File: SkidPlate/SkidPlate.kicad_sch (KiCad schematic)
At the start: 23 parts, among them J8 S4B-PH-SM4-TB, U1 AMS1117-3.3, U2 LSM6DSOX

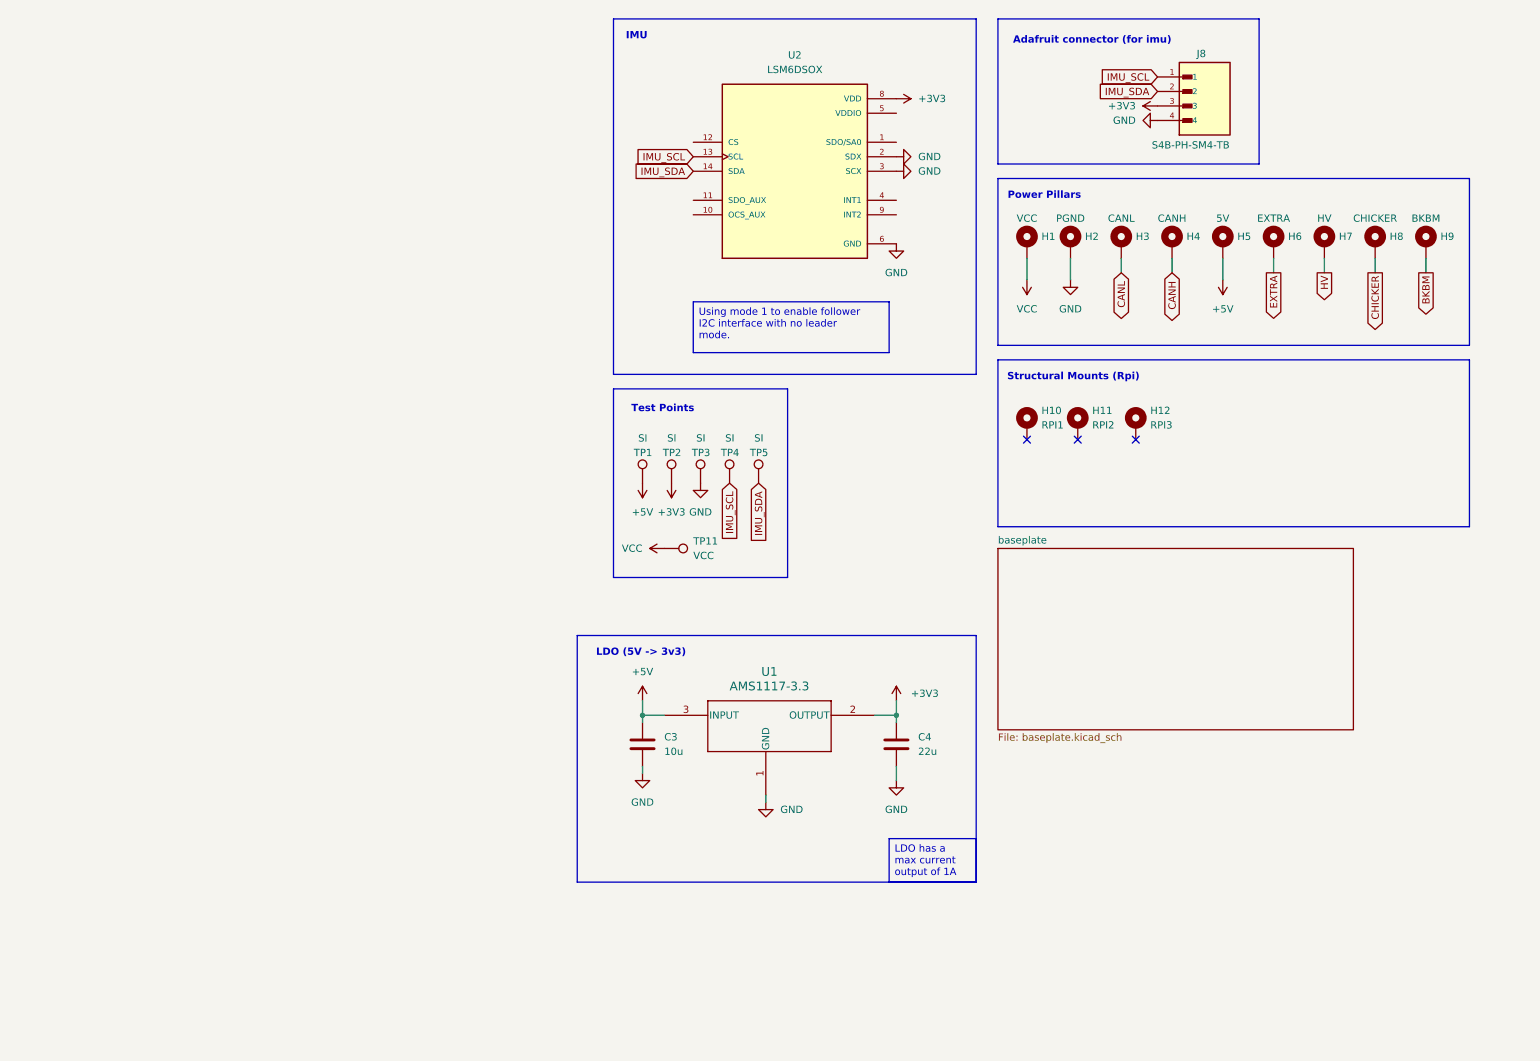
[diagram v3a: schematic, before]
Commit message: skidplate
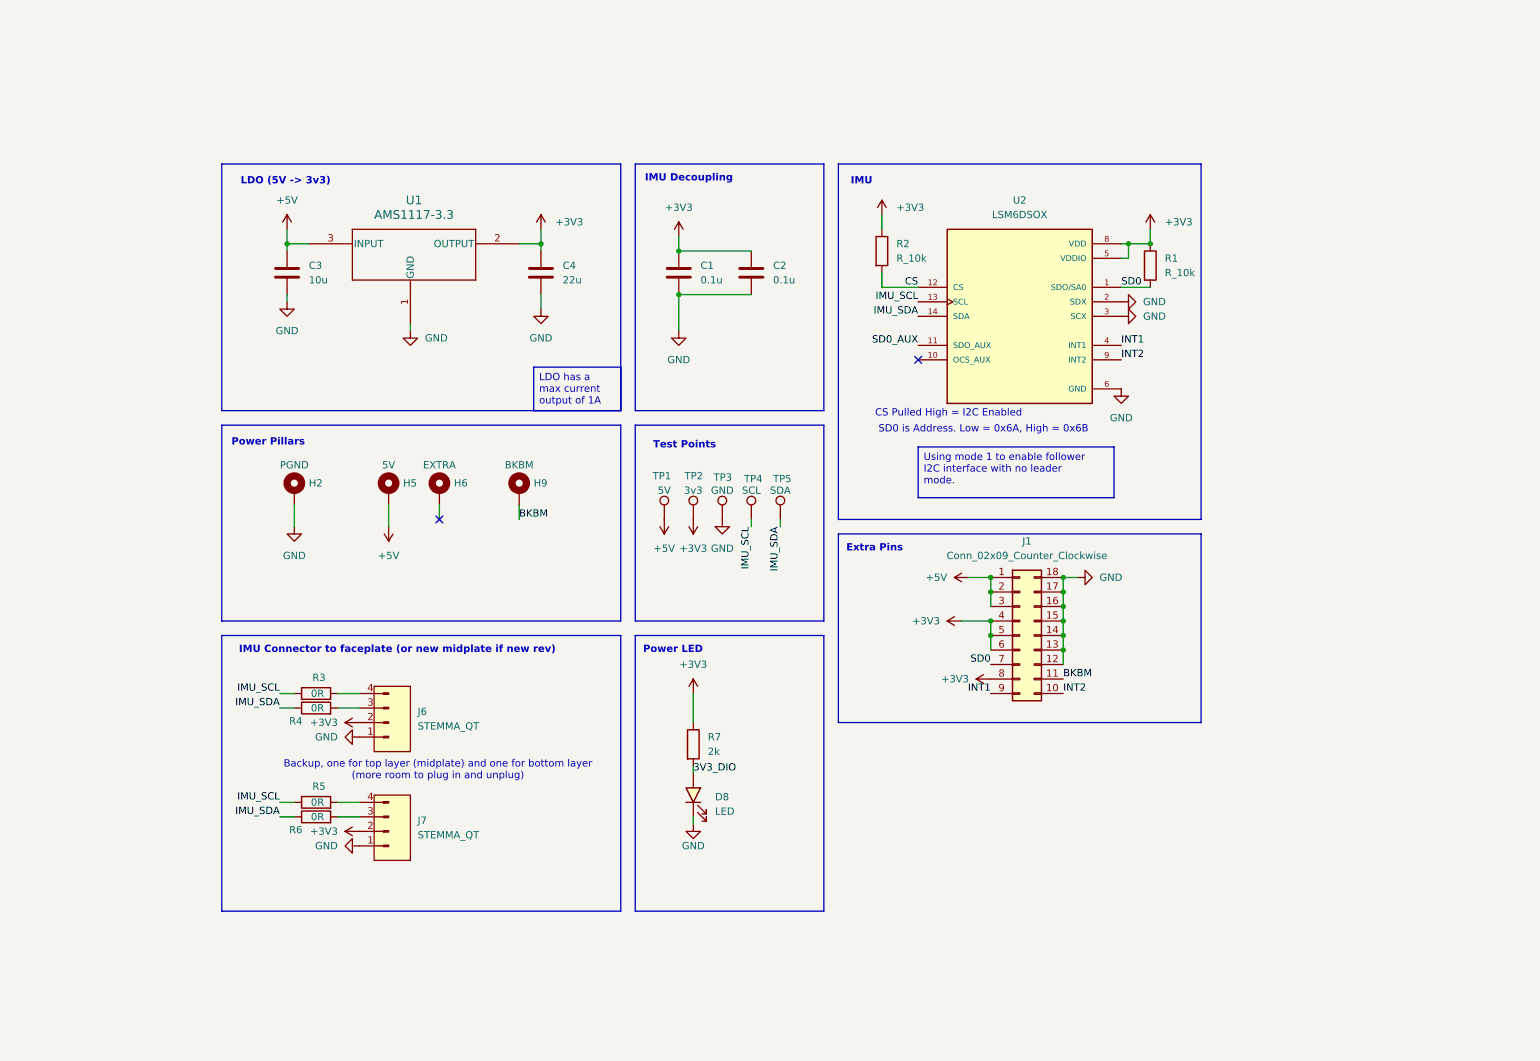
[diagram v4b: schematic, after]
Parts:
- removed H1: VCC, bots:MountingHole_2.7mm_M2.5_DIN965_Pad, symbol bots:MountingHoleM2.5NoThread_wConn
- removed H10: RPI1, bots:MountingHole_2.7mm_M2.5_DIN965_Pad, symbol bots:MountingHoleM2.5NoThread_wConn
- removed H11: RPI2, bots:MountingHole_2.7mm_M2.5_DIN965_Pad, symbol bots:MountingHoleM2.5NoThread_wConn
- removed H12: RPI3, bots:MountingHole_2.7mm_M2.5_DIN965_Pad, symbol bots:MountingHoleM2.5NoThread_wConn
- removed H3: CANL, bots:MountingHole_2.7mm_M2.5_DIN965_Pad, symbol bots:MountingHoleM2.5NoThread_wConn
- removed H4: CANH, bots:MountingHole_2.7mm_M2.5_DIN965_Pad, symbol bots:MountingHoleM2.5NoThread_wConn
- removed H7: HV, bots:MountingHole_2.7mm_M2.5_DIN965_Pad, symbol bots:MountingHoleM2.5NoThread_wConn
- removed H8: CHICKER, bots:MountingHole_2.7mm_M2.5_DIN965_Pad, symbol bots:MountingHoleM2.5NoThread_wConn
- removed J8: S4B-PH-SM4-TB, S4B-PH-SM4-TB:JST_S4B-PH-SM4-TB, symbol bots:S4B-PH-SM4-TB
- removed TP11: VCC, bots:TestPoint_Pad_2.0x2.0mm, symbol bots:TestPoint_2x2
- added C1, C2: 0.1u, bots:C_0603_1608Metric, symbol bots:C_0.1u
- added D8: LED, bots:LED_0805_2012Metric, symbol bots:LED_green
- added J1: Conn_02x09_Counter_Clockwise, bots:PinHeader_2x09_P2.54mm_Vertical, symbol bots:Conn_02x09_Counter_Clockwise
- added J6, J7: STEMMA_QT, bots:JST_SH_BM04B-SRSS-TB_1x04-1MP_P1.00mm_Vertical, symbol bots:STEMMA_QT
- added R1, R2: R_10k, bots:R_0603_1608Metric, symbol bots:R_10k
- added R3, R4, R5, R6: 0R, bots:R_0603_1608Metric, symbol bots:R_0R
- added R7: 2k, bots:R_0603_1608Metric, symbol bots:R_2k
- TP1: value SI -> 5V; footprint bots:pad_0603 -> bots:TestPoint_Pad_D1.0mm; symbol bots:TestPoint_1x1 -> bots:TestPoint1.0mm; now in the parts list
- TP2: value SI -> 3v3; footprint bots:pad_0603 -> bots:TestPoint_Pad_D1.0mm; symbol bots:TestPoint_1x1 -> bots:TestPoint1.0mm; now in the parts list
- TP3: value SI -> GND; footprint bots:pad_0603 -> bots:TestPoint_Pad_D1.0mm; symbol bots:TestPoint_1x1 -> bots:TestPoint1.0mm; now in the parts list
- TP4: value SI -> SCL; footprint bots:pad_0603 -> bots:TestPoint_Pad_D1.0mm; symbol bots:TestPoint_1x1 -> bots:TestPoint1.0mm; now in the parts list
- TP5: value SI -> SDA; footprint bots:pad_0603 -> bots:TestPoint_Pad_D1.0mm; symbol bots:TestPoint_1x1 -> bots:TestPoint1.0mm; now in the parts list
- U2: footprint bots:PQFN50P300X250X86-14N -> bots:PQFN50P250X300X86-14N; JLC (none) -> LGA-14(2.5x3); LCSC (none) -> C2655100
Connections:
- net +3V3: now also U2.5 (VDDIO), C1.1, C2.1, J1.4 (Pin_4), J1.5 (Pin_5), J1.6 (Pin_6), J1.8 (Pin_8), J6.2 (Pin_2), J7.2 (Pin_2), R1.1, R2.1, R7.1
- net +5V: now also J1.1 (Pin_1), J1.2 (Pin_2), J1.3 (Pin_3)
- net BKBM: now also J1.11 (Pin_11)
- net GND: now also C1.2, C2.2, D8.1 (K), J1.12 (Pin_12), J1.13 (Pin_13), J1.14 (Pin_14), J1.15 (Pin_15), J1.16 (Pin_16), J1.17 (Pin_17), J1.18 (Pin_18), J6.1 (Pin_1), J7.1 (Pin_1)
- net IMU_SCL: now also R3.1, R5.1
- net IMU_SDA: now also R4.1, R6.1
- net SD0: now reaches U2.1 (SDO/SA0)
- net SD0: now also J1.7 (Pin_7), R1.2
- net SD0_AUX: now reaches U2.11 (SDO_AUX)
- net CS: now reaches U2.12 (CS)
- net CS: now also R2.2
- net INT1: now reaches U2.4 (INT1)
- net INT1: now also J1.9 (Pin_9)
- net INT2: now reaches U2.9 (INT2)
- net INT2: now also J1.10 (Pin_10)
- net EXTRA: no longer names the net of H6.1
- new net: J6.3 (Pin_3), R4.2
- new net: J6.4 (Pin_4), R3.2
- new net: J7.3 (Pin_3), R6.2
- new net: J7.4 (Pin_4), R5.2
- new net 3V3_DIO: D8.2 (A), R7.2
- no-connect marks 3 -> 2
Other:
- removed sheet baseplate
- note added: "Backup, one for top layer (midplate) and one for bottom layer (more room to plug in and unplug)"
- note added: "CS Pulled High = I2C Enabled"
- note added: "Extra Pins"
- note added: "IMU Connector to faceplate (or new midplate if new rev)"
- note added: "IMU Decoupling"
- note added: "Power LED"
- note added: "SD0 is Address. Low = 0x6A, High = 0x6B"
- note removed: "Adafruit connector (for imu)"
- note removed: "Structural Mounts (Rpi)"
- moved on the sheet: C3, C4, H2, H5, H6, H9, TP1, TP2, TP3, TP4, TP5, U1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

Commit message: skidplate done
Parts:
- removed H6: EXTRA, bots:MountingHole_2.7mm_M2.5_DIN965_Pad, symbol bots:MountingHoleM2.5NoThread_wConn
- removed H9: BKBM, bots:MountingHole_2.7mm_M2.5_DIN965_Pad, symbol bots:MountingHoleM2.5NoThread_wConn
- added H1: RPI, bots:MountingHole_2.7mm_M2.5_DIN965_Pad, symbol bots:MountingHoleM2.5NoThread_wConn
- added H3: CANH, bots:MountingHole_2.7mm_M2.5_DIN965_Pad, symbol bots:MountingHoleM2.5NoThread_wConn
- renumbered H5 to H2, H2 to H5
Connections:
- net BKBM is gone; now on net +3V3: J1.11 (Pin_11)
- new net CANH: H3.1
- no-connect marks 2 -> 3
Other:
- moved on the sheet: H2, H5
